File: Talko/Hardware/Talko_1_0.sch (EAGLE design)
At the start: 64 parts, among them IC1 MEGA8-AI, IC2 4511D, IC3 7824DT, IC5 MCP2200, J1 AVR_SPI_PRG_62X3_LOCK, Q1 16 MHz, X3 USB

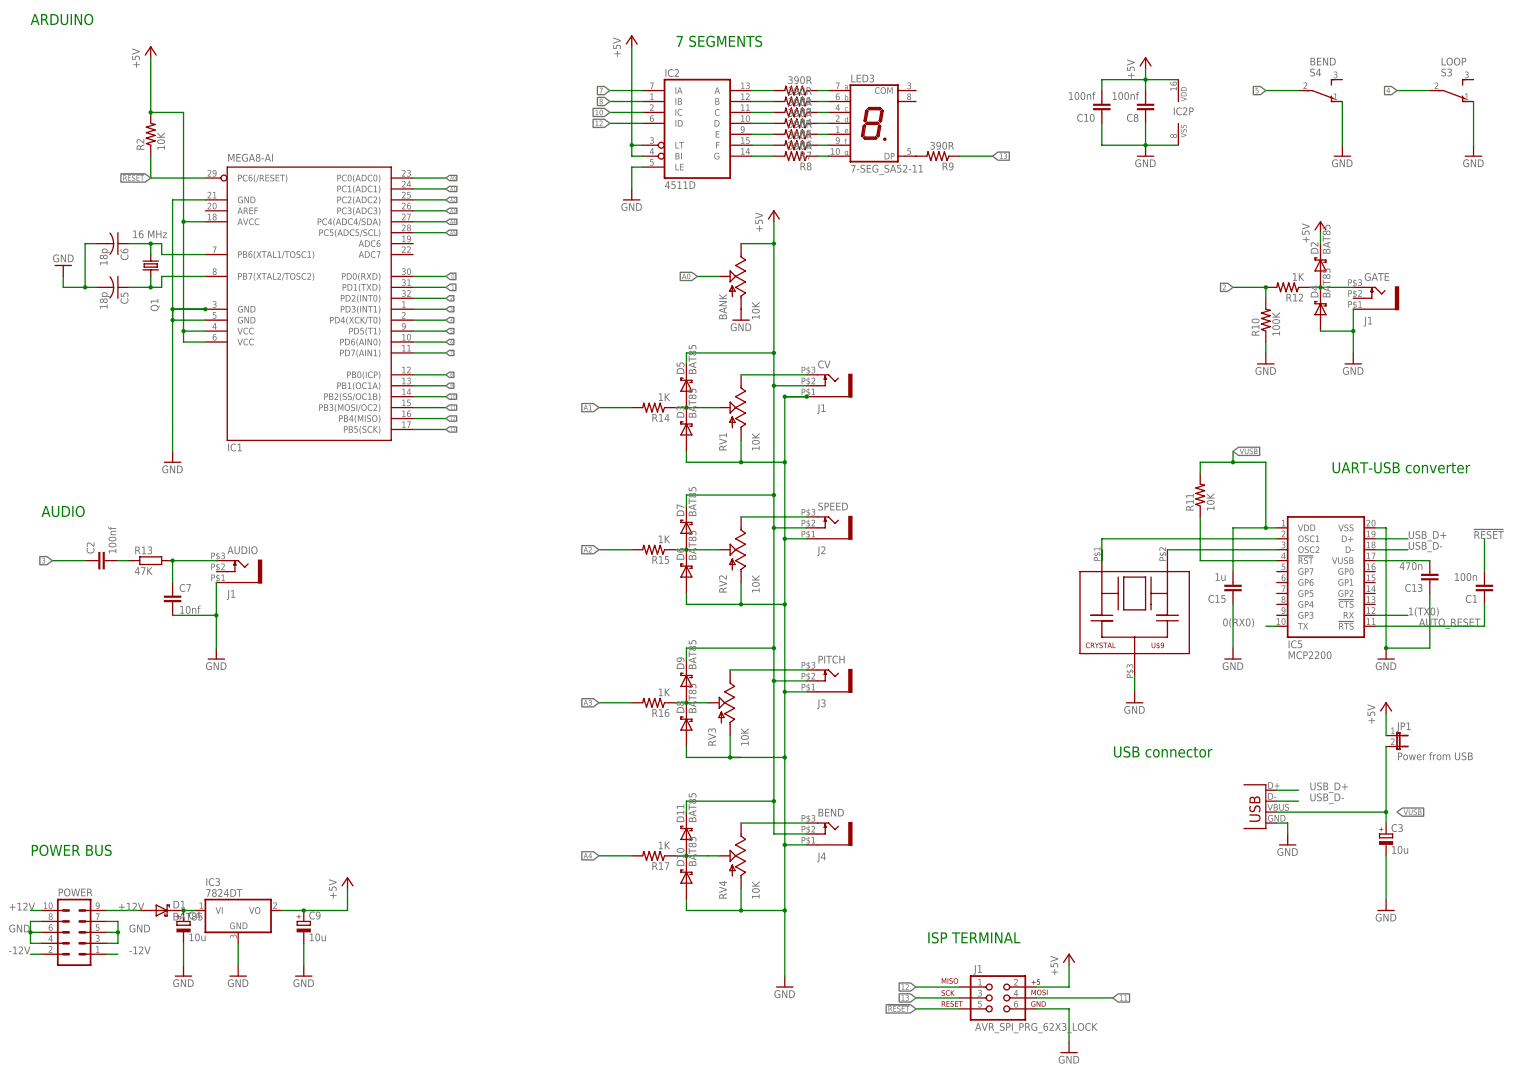
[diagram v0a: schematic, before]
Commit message: Talkie renamed to Talko Talko Schematic Added female voice
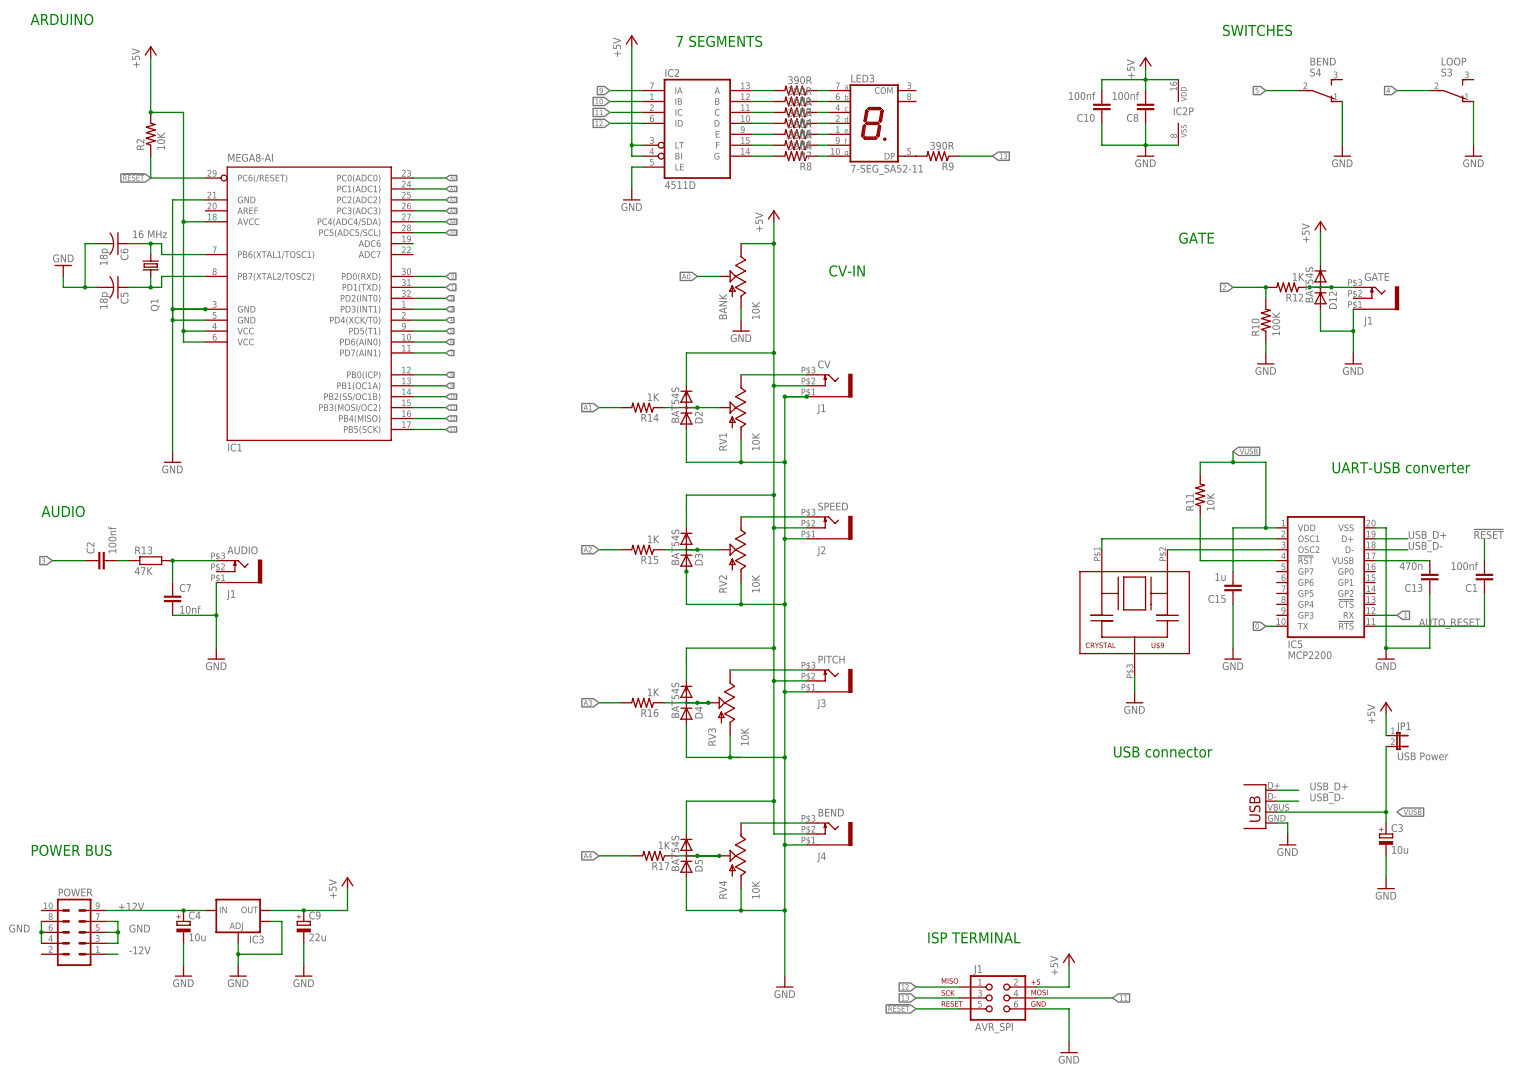
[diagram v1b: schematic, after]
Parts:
- removed D1, D10, D11, D6, D7, D8, D9: BAT85, SteveMarple:DIODE-SCHOTTKY_
- added D12: BAT54S, diode:DIODE_2CACA-SOT23
- C1: value 100n -> 100nf; device SparkFun:CAP0805 -> resistor:C-EUC0805; OC_FARNELL 1216438 -> (none)
- C9: value 10u -> 22u
- D2, D3, D4, D5: value BAT85 -> BAT54S; device SteveMarple:DIODE-SCHOTTKY_ -> diode:DIODE_2CACA-SOT23; OC_FARNELL 1612329 -> (none)
- IC3: value 7824DT -> (none); device linear:7824DT -> SparkFun-PowerIC:V_REG_LM1117SOT223; OC_MOUSER (none) -> 998-MIC5205-5.0YM5TR
- J1: value AVR_SPI_PRG_62X3_LOCK -> AVR_SPI
- JP1: value Power from USB -> USB Power
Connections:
- removed net 0(RX0): IC5.TX
- removed net 1(TX0): IC5.RX
- removed net N$32: D6.C, D7.A, R15.1, RV2.S
- removed net N$35: D8.C, D9.A, R16.1, RV3.S
- removed net N$38: D10.C, D11.A, R17.1, RV4.S
- removed net N$6: C4.+, D1.C, IC3.VI
- new net N$30: D4.AC, R16.1, RV3.S
- new net N$33: D5.AC, R17.1, RV4.S
- net +12V: now also C4.+, IC3.IN; no longer D1.A, POWER.10
- net +5V: now also D12.C, D3.C, D4.C, IC3.OUT; no longer D11.C, D7.C, D9.C, IC3.VO
- net -12V: no longer POWER.2
- net 0: now also IC5.TX
- net 1: now also IC5.RX
- net 10: now also IC2A.IB; no longer IC2A.IC
- net 11: now also IC2A.IC
- net 7: no longer IC2A.IA
- net 8: no longer IC2A.IB
- net 9: now also IC2A.IA
- net GND: now also C3.-, D12.A, D2.A, D5.A, IC3.ADJ, IC3.OUT@1; no longer D10.A, D6.A, D8.A, IC3.GND
- net N$1: now also D12.AC, GATE.3, R12.1; no longer C3.-
- net N$31: now also D3.AC, R15.1, RV2.S; no longer D2.A, D4.C, GATE.3, R12.1
- net N$9: now also D2.AC; no longer D3.C, D5.A
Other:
- note added: "CV-IN"
- note added: "GATE"
- note added: "SWITCHES"
- moved on the sheet: C1, R14, R15, R16

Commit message: adding schematic image file to Talko
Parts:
- BANK, RV1, RV2, RV3, RV4: OC_MOUSER (none) -> 688-RK09L1140A2U
- C1: OC_FARNELL (none) -> 77-VJ0805V104MXBPBC
- C10, C8: OC_MOUSER (none) -> 77-VJ0805V104MXBPBC
- C4, C9: OC_MOUSER (none) -> 581-F981C106MSAAS1
- C6: OC_MOUSER (none) -> 77-VJ0805A180GXQCBC
- IC1: OC_MOUSER (none) -> 556-ATMEGA328P-AU
- IC2: OC_MOUSER (none) -> 863-MC14511BDG
- IC3: OC_MOUSER 998-MIC5205-5.0YM5TR -> 621-AZ1117H-5.0TRE
- IC5: OC_MOUSER (none) -> 579-MCP2200-I/SO

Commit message: Fixing a bug in loop mode changing switch reference @ Mouser (for a bigger lever)
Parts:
- C1: OC_FARNELL 77-VJ0805V104MXBPBC -> (none); OC_MOUSER (none) -> 77-VJ0805V104MXBPBC
- C13: OC_MOUSER (none) -> 77-VJ0805Y474KXQTBC
- C15: OC_MOUSER (none) -> 77-VJ0805Y105KXQTBC
- C2: OC_FARNELL (none) -> 77-VJ0805V104MXBPBC
- C3: OC_MOUSER (none) -> 581-F981C106MSAAS1
- C5: OC_MOUSER (none) -> 77-VJ0805A180GXQCBC
- C7: OC_MOUSER (none) -> 77-VJ0805Y103JXAPBC
- C9: value 22u -> 10u
- D12, D2, D3, D4, D5: OC_MOUSER (none) -> 78-BAT54S-E3-08
- J1: OC_MOUSER (none) -> 571-826925-3
- JP1: OC_MOUSER (none) -> 571-826646-2
- LED3: OC_MOUSER (none) -> 604-SC52-11SRWA
- POWER: OC_MOUSER (none) -> 571-5-146258-5
- Q1: OC_MOUSER ECS-160-18-23A-EN-TR -> 774-406C35S16M00000
- R1, R3, R4, R5, R6, R7, R8, R9: OC_MOUSER (none) -> 754-RR1220P-391D
- R10: value 100K -> 10K; OC_MOUSER (none) -> 754-RR1220P-103D
- R11, R2: OC_MOUSER (none) -> 754-RR1220P-103D
- R12, R14, R15, R16, R17: OC_MOUSER (none) -> 71-TNPW08051K00BEEA
- R13: OC_MOUSER (none) -> 754-RR1220P-473D
- S3, S4: OC_MOUSER (none) -> 612-200ASP1T1A1M2R
- X3: 0C_FARNELL 1308876 -> (none); OC_MOUSER (none) -> 855-M701-330442
